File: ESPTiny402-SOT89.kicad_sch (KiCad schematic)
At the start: 18 parts, among them J1 Conn_01x10_Male, J2 Conn_01x10_Male, J3 Conn_01x04_Male, U1 ESP-01v090, U2 ATtiny402-SS, U3 MCP1700

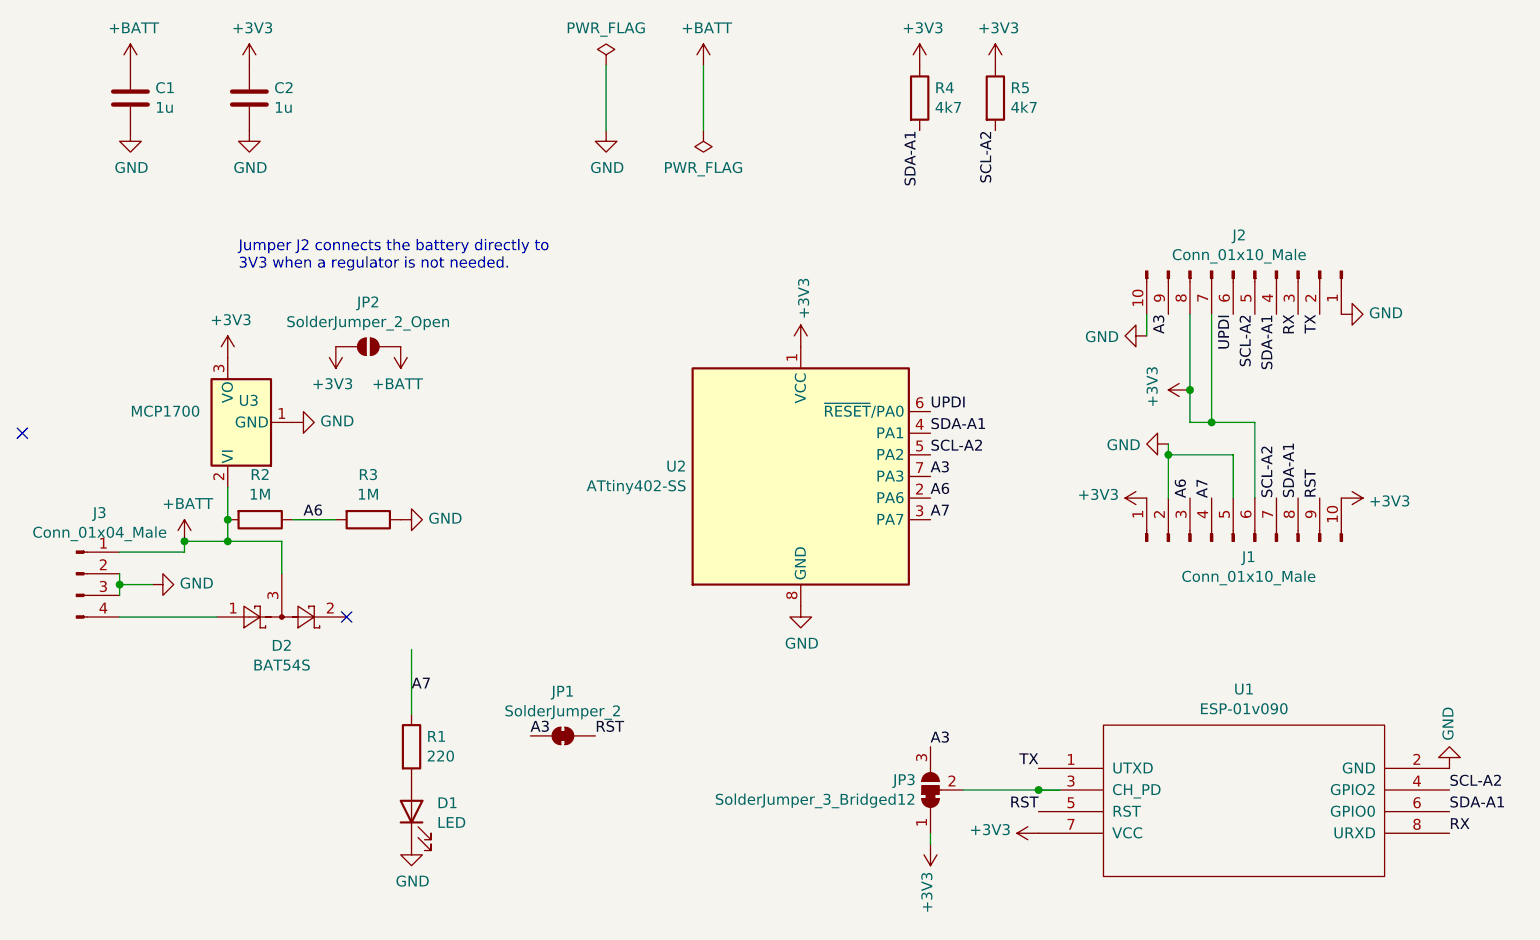
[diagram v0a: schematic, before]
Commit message: Minor cosmetic cleanups
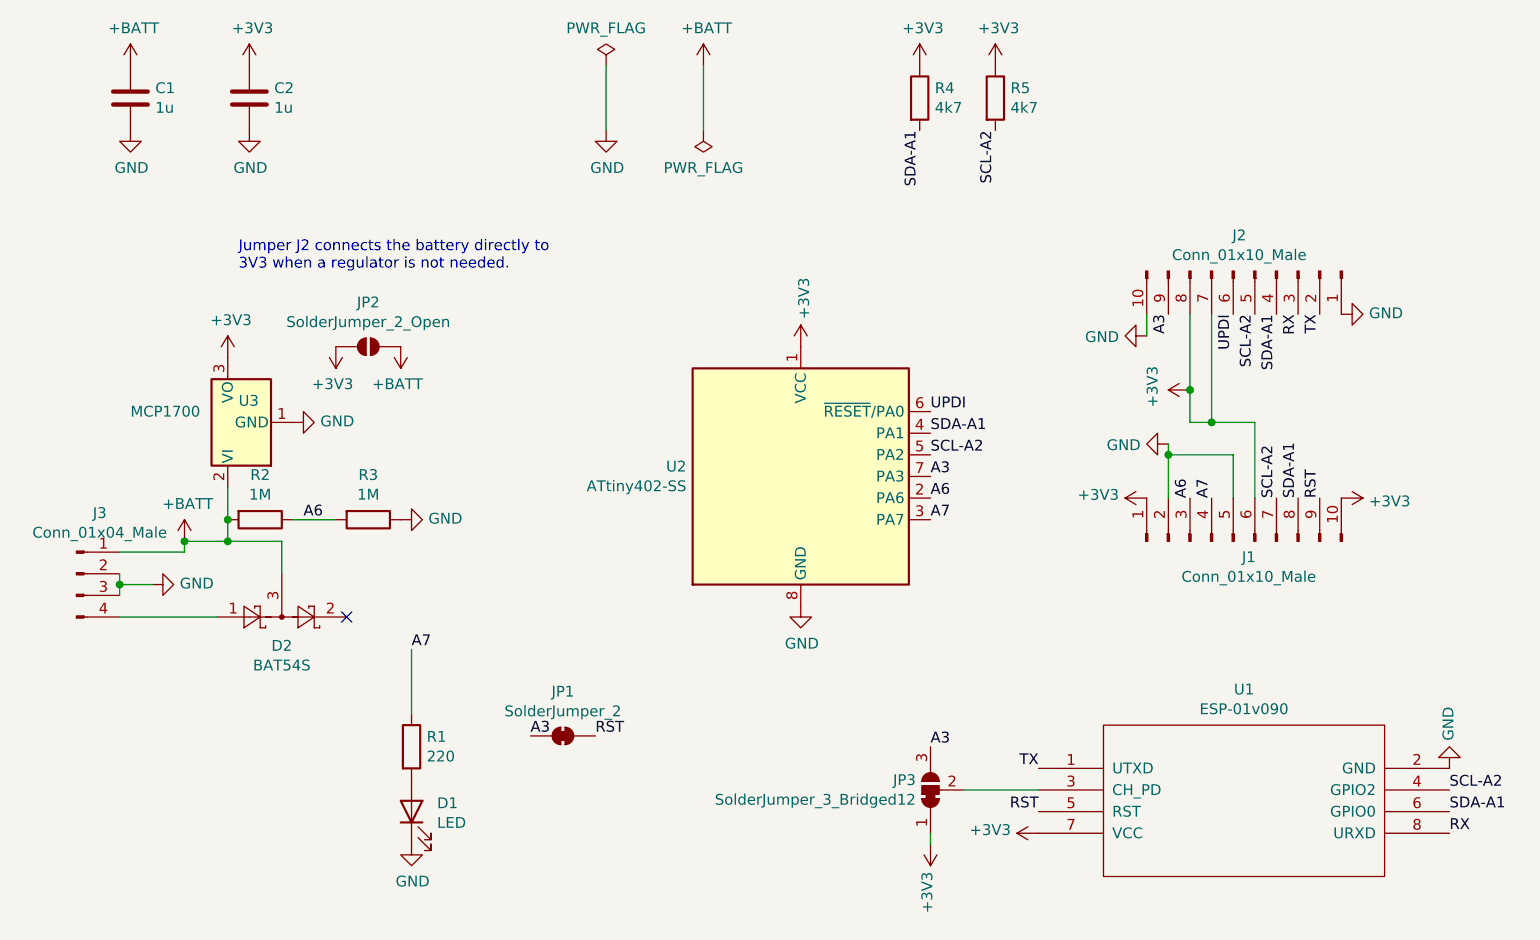
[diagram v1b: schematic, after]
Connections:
- no-connect marks 2 -> 1
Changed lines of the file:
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@@
-	)
-	(junction
-		(at 147.32 116.84)
-		(diameter 0)
-		(color 0 0 0 0)
 	)
 	(junction
@@
 		(at 66.04 96.52)
 	)
-	(no_connect
-		(at 27.94 74.93)
-	)
 	(wire
 		(pts
@@
 		(pts
 			(xy 134.62 123.19) (xy 134.62 121.92)
-		)
-		(stroke
-			(width 0)
-			(type default)
-		)
-	)
-	(wire
-		(pts
-			(xy 149.86 116.84) (xy 147.32 116.84)
 		)
 		(stroke
@@
 	)
 	(label "A7"
-		(at 73.66 105.41 0)
-		(effects
-			(font
+		(at 73.66 100.33 0)
+		(effects
+			(font
